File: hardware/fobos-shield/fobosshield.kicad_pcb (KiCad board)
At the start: 4 copper layers, 76.2 x 71.1 mm, 170 parts, among them J1 Target, J10 ADCin, J11 PP1, J12 PP2, J13 Clock, J14 Trigger, J15 CSM5VCur, J16 Conn_01x01, J17 Barrel_Jack_Switch, J18 Conn_01x02, J19 Conn_01x02, J2 Glitch, J20 CSM3V3Cur, J21 GND, J22 GND, J23 CSM5VCur, J24 Conn_01x02, J25 V_Var, J26 AUX, J27 GNDP, J3 Analog, J4 IOH, J5 SPI, J6 Analog2, J7 Power, J8 IOL, J9 SPI2, Q1 IRF7807Z, Q2 IRLML2502, Q3 BSS138L, U1 RB-0509D, U10 INA225, U11 INA225, U12 LD1117S33TR_SOT223, U13 INA225, U2 REE-0505S, U3 LM317L_SO8, U4 LM337L_SO8, U5 LD59015, U6 LP3985IM5-3.0, U7 AD8331, U8 TPS7A7100_VQFN20, U9 AD9215

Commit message: FBOBOS Shield rev2 passes DRC
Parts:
- moved U10 0.51 mm to (59.4, 54.1)
- moved R28 0.51 mm to (56.4, 54.2)
- moved C54 0.48 mm to (59.4, 58.2)
- moved R38 0.25 mm to (49.5, 64.3)
- moved C56 0.13 mm to (49.5, 77.7)
- moved R37 0.13 mm to (66.1, 64.9)
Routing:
- net (no net): track 0.00 -> 14.2 mm, vias 0 -> 6
- net GND: track 116.6 -> 126.8 mm, vias 51 -> 134
- net 5Vclean: track 12.7 -> 18.2 mm
- net FC_3V3: track 118.8 -> 121.0 mm
- net VCC5V0: track 102.0 -> 103.7 mm
- net FC_5V: track 146.2 -> 147.6 mm
- net GNDA: track 132.5 -> 133.7 mm, vias 31 -> 49
- net CSM5VCur: track 58.1 -> 57.6 mm
- net CSM5VGain1: track 54.1 -> 53.6 mm
- net CSM5VGain0: track 56.0 -> 55.5 mm
- net /Power/GNDP: track 137.7 -> 137.8 mm, vias 20 -> 17
- added copper zone on In2.Cu, net FC_3V3
- added copper zone on In2.Cu, net FC_5V
- added copper zone on B.Cu, net GND
- added copper zone on F.Cu, net GND
- added copper zone on In2.Cu, net GND
- added copper zone on In2.Cu, net IN
- added copper zone on In2.Cu, net VCC3V3
- added copper zone on In2.Cu, net VCC5V0
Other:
- net class Default: via_dia 0.508 -> 0.6858; via_drill 0.254 -> 0.3302
- rule solder_mask_min_width: 0.25 -> 0.1016
- rule trace_min: 0.1524 -> 0.127
- rule via_min_size: 0.508 -> 0.4572

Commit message: ready for review
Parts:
- moved D9 0.57 mm to (70.4, 55.6)
- moved D10 0.25 mm to (70.4, 79.8)
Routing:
- net CSMVarCur: track 33.3 -> 37.0 mm
- net CSM3V3Cur: track 16.1 -> 16.8 mm
- net Net-(D9-Pad2): track 4.13 -> 3.52 mm
- net CSM5VGain1: track 53.6 -> 54.1 mm
- net CSM5VCur: track 57.6 -> 57.0 mm
- net GND: vias 134 -> 131

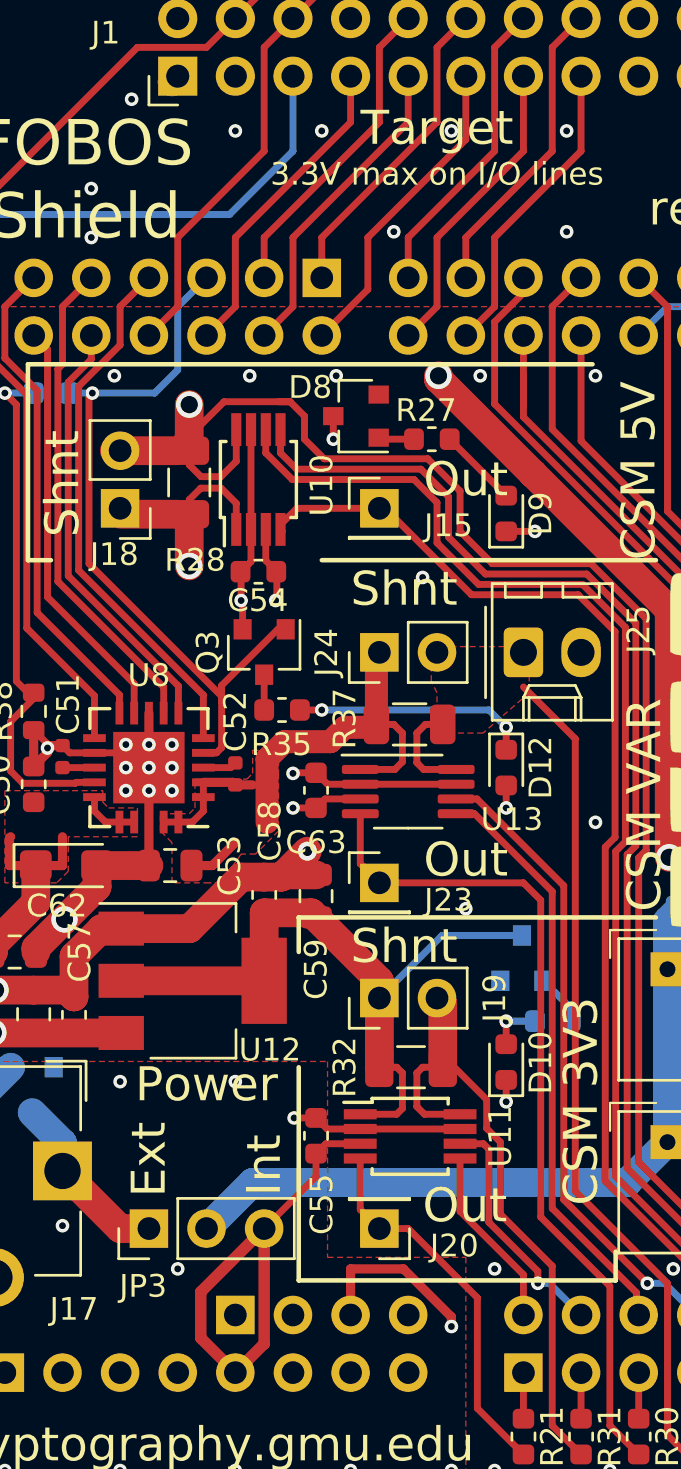
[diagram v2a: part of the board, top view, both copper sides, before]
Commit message: disconnected XADC ground from GND
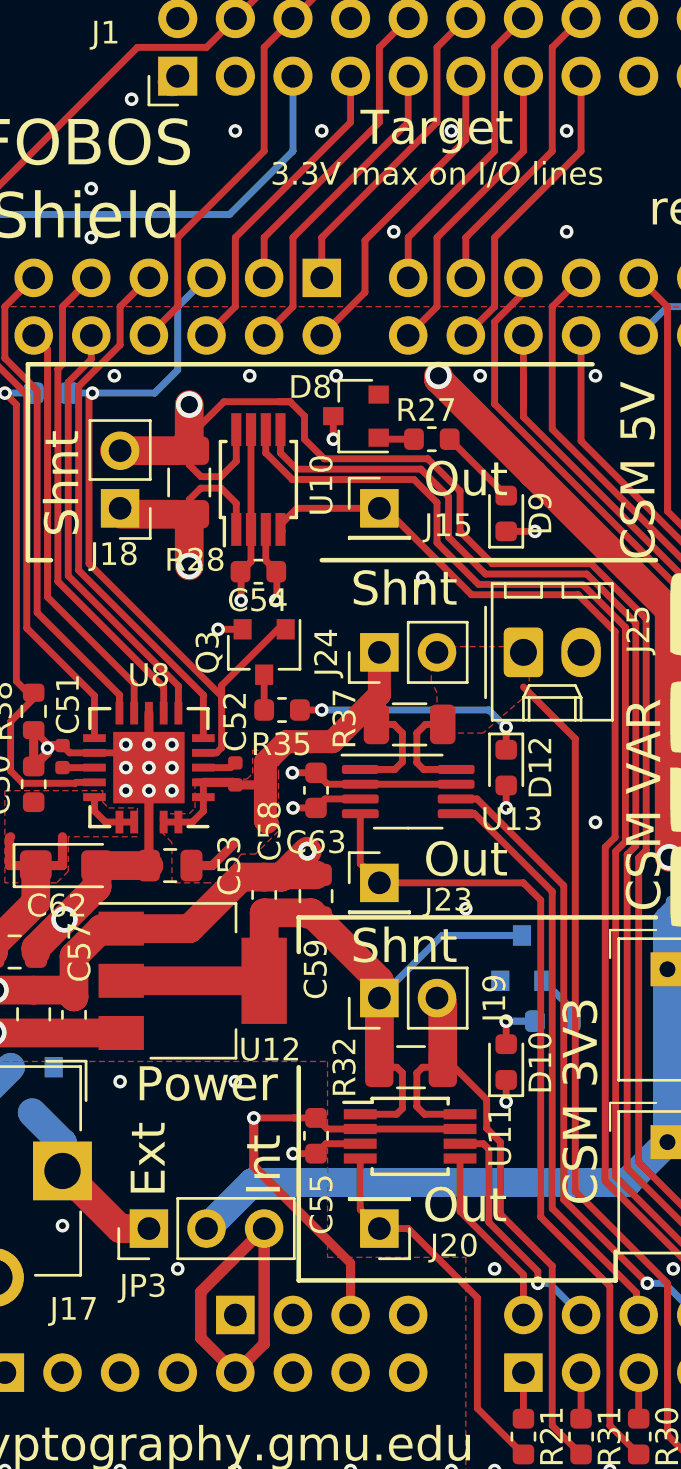
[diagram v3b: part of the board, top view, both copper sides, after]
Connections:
- C54 pad 2: GND -> XADCGND
- C55 pad 2: GND -> XADCGND
- C63 pad 2: GND -> XADCGND
- J6 pad 3: GND -> XADCGND
- U10 pad 2: GND -> XADCGND
- U10 pad 7: GND -> XADCGND
- U11 pad 2: GND -> XADCGND
- U11 pad 7: GND -> XADCGND
- U13 pad 2: GND -> XADCGND
- U13 pad 7: GND -> XADCGND
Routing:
- net XADCGND: track 0.00 -> 59.6 mm, vias 0 -> 3
- net GND: track 126.8 -> 96.2 mm, vias 131 -> 128
- net VCC5V0: track 103.7 -> 100.5 mm, vias 3 -> 4
- net Net-(C52-Pad1): track 23.9 -> 25.2 mm

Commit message: fixed small PCB problems
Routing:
- net (no net): track 14.2 -> 0.00 mm, vias 6 -> 0
- net /Power/GNDP: track 137.8 -> 149.8 mm, vias 17 -> 24
- net VCC5V0: track 100.5 -> 103.9 mm

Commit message: small PCB improvements
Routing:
- net FC_5V: track 147.8 -> 166.8 mm
- net GND: track 96.2 -> 101.0 mm, vias 128 -> 130
- net IN: track 129.0 -> 130.8 mm

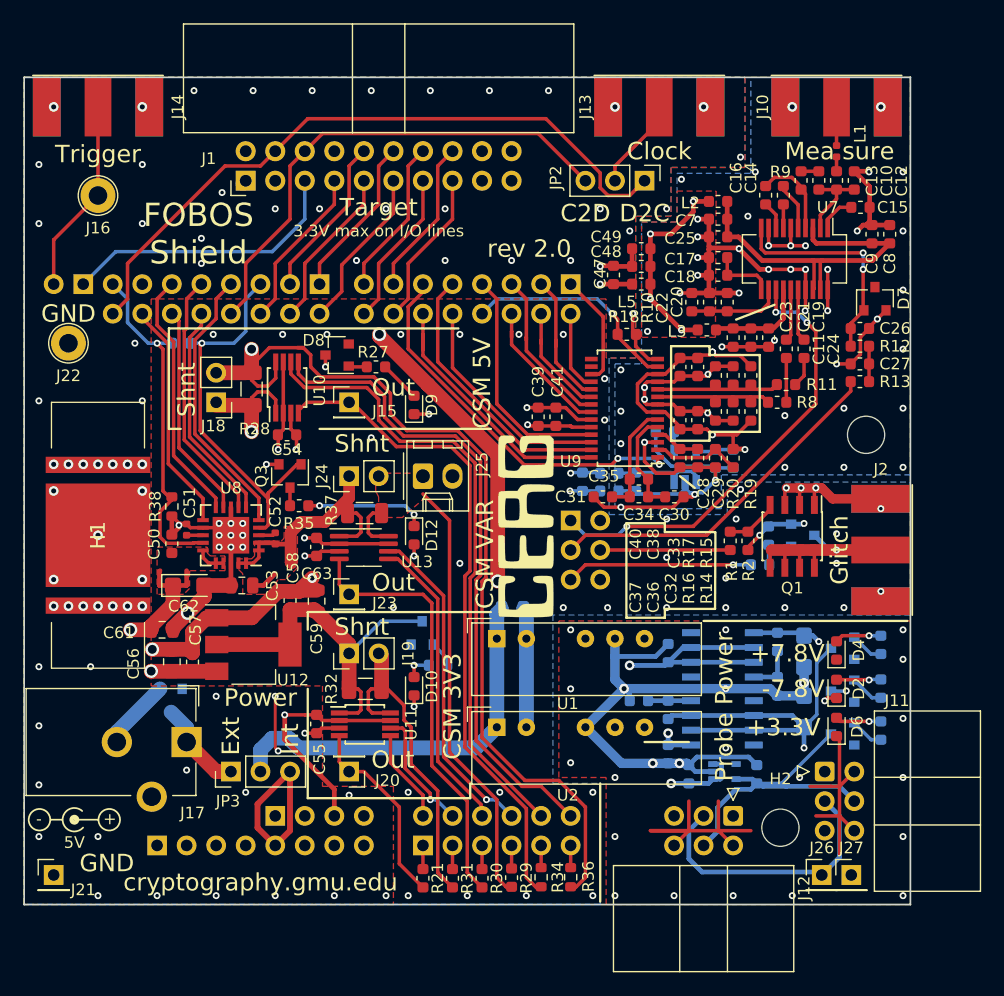
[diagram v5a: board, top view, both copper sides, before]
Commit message: added SMA for input from INA225 on DUT
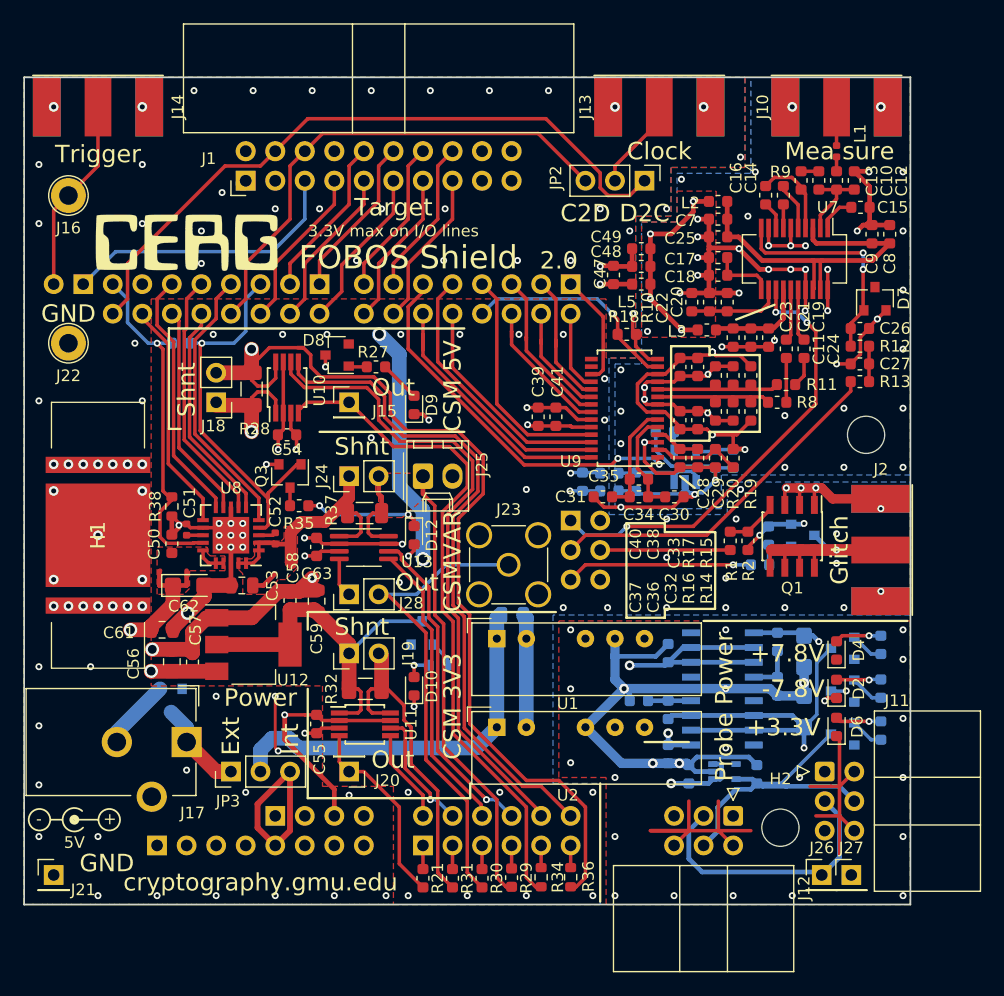
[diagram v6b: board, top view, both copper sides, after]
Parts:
- added J28: CSM5VCur, Connector_PinHeader_2.54mm:PinHeader_1x02_P2.54mm_Vertical, F.Cu at (64.8, 71.9)
- J23: value CSM5VCur -> Conn_Coaxial_Power; footprint Connector_PinHeader_2.54mm:PinHeader_1x01_P2.54mm_Vertical -> Connector_Coaxial:SMA_Amphenol_901-144_Vertical
- moved G*** 38.1 mm to (50.8, 41.7), turned to 0 degrees
- moved J23 13.9 mm to (78.5, 69.3)
- moved J16 2.54 mm to (40.6, 37.6)
- moved C60 0.51 mm to (78.8, 73.7)
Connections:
- U13 pad 4: CSMVarCur -> Net-(J28-Pad1)
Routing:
- net XADCGND: track 59.6 -> 95.7 mm, vias 3 -> 4
- net VCC3V3: track 79.9 -> 88.3 mm
- net FC_3V3: track 121.1 -> 113.4 mm
- net FC_Var: track 42.0 -> 46.8 mm
- net CSMVarCur: track 37.0 -> 41.6 mm
- net Net-(J28-Pad1): track 0.00 -> 3.40 mm
- net FC_5V: track 166.8 -> 168.2 mm
- net CSM5VGain0: track 55.8 -> 57.2 mm
- net CSM5VGain1: track 54.1 -> 55.5 mm
- net CSM5VCur: track 57.0 -> 58.4 mm
- net IN: track 130.8 -> 130.2 mm
- net GND: track 101.0 -> 100.7 mm, vias 130 -> 129
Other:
- board text added: "2.0"
- board text added: "CSMVAR"
- board text removed: "CSM VAR"
- board text removed: "rev 2.0"

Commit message: FOBOS Shield rev2 ready for manufacturing
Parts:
- removed H2: MountingHole, MountingHole:MountingHole_3.2mm_M3
- H3: footprint MountingHole:MountingHole_3.2mm_M3 -> MountingHole:MountingHole_3.2mm_M3_DIN965_Pad_TopBottom
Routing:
- net GND: track 100.7 -> 131.4 mm
- net XADCGND: track 95.7 -> 90.9 mm
- net /Power/3V3P: track 27.1 -> 25.9 mm
- net /Power/+7V8P: track 42.9 -> 44.1 mm, vias 1 -> 0
- added copper zone on In2.Cu, net GNDA
- removed copper zone on In2.Cu, net 5Vclean

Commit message: last PCB update before shipping
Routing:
- net IN: track 130.2 -> 137.4 mm
